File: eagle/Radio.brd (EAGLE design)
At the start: 100 x 80 mm, 134 parts, among them J500 2060-402, J501 2060-402, J920 2060-402, J921 2060-402, Q210 32.768kHz, Q610 32.768kHz, Q900 BSS123, U100 LP38693, U200 MSP430G2553, U300 IRF7103, U500 TPA2016D2, U900 EA_DOGMXXX-A, U910 PCA8574, U920 PCA9632TK, U930 IRF7309, U940 OPT3001, X100 2510-5, X110 2510-5

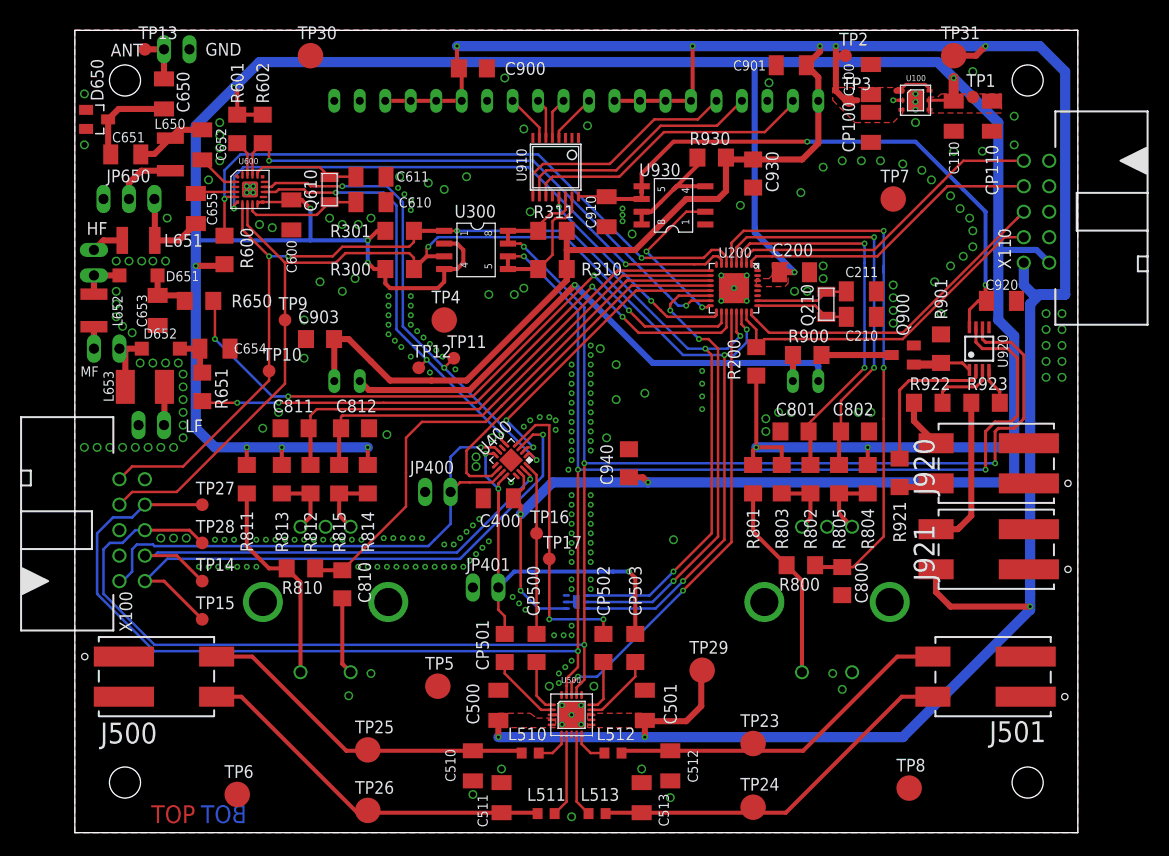
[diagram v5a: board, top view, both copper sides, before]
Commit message: CHG: updated libary pathes for all non standart components to Radio Projekt.lbr
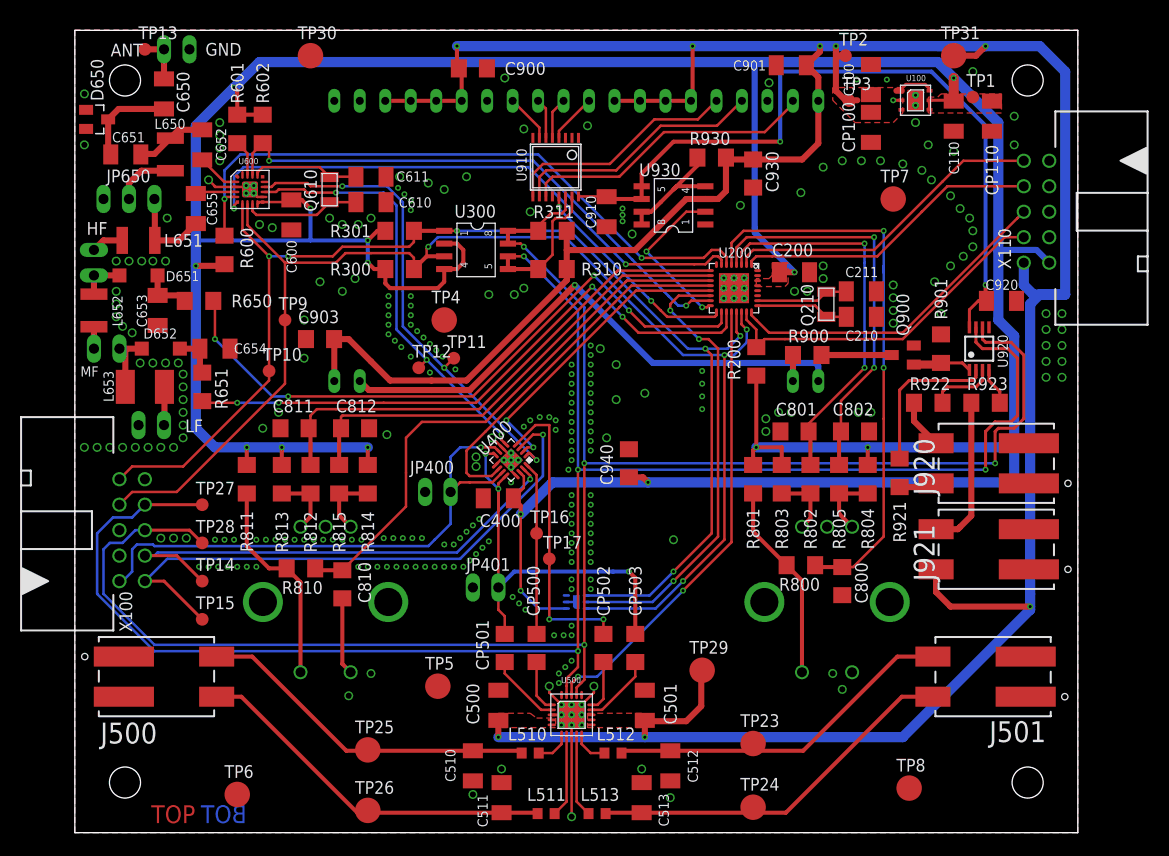
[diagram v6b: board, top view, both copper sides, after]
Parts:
- J500, J501, J920, J921: device Wago-2060-402:WAGO_2060-402 -> Radio Projekt:WAGO_2060-402
- R602: value 10k -> DNB
- U400: device TI_Radio:QFN16 -> Radio Projekt:QFN16
- U600: device SI473X-D60:SI473X-D60 -> Radio Projekt:SI473X-D60
- U920: device NXP_By_element14_Batch_1:TSSOP8 -> Radio Projekt:TSSOP8
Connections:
- net GND: now also U100.EXP1, U100.EXP2, U200.TP1, U200.TP2, U200.TP3, U200.TP4, U200.TP5, U200.TP6, U200.TP7, U200.TP8, U200.TP9, U400.TH, U400.TH1, U400.TH2, U400.TH3, U400.TH4, U400.TH5, U500.EXP1, U500.EXP2, U500.EXP3, U500.EXP4, U500.EXP5, U500.EXP6, U500.EXP7, U500.EXP8, U500.EXP9, U600.GND-PAD1, U600.GND-PAD2, U600.GND-PAD3, U600.GND-PAD4
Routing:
- net GND: track 11.5 -> 39.8 mm, vias 293 -> 278
- net +5_PCA: track 61.2 -> 75.0 mm

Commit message: CHG: added some testpads for debugging methode
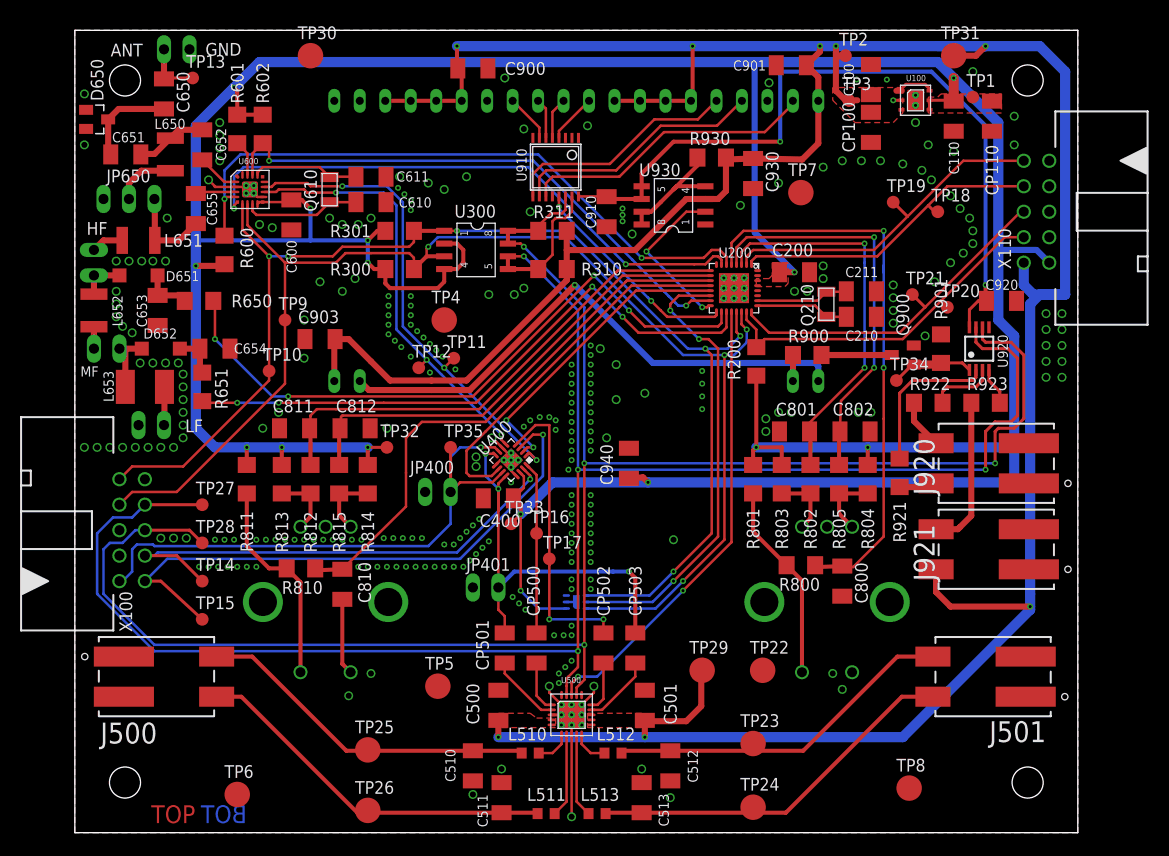
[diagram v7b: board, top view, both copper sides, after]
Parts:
- added TP18, TP19, TP20, TP21, TP32, TP33, TP34, TP35: PTR1B1,27, testpad:B1,27
- added TP22: PTR1B2,54, testpad:B2,54
- C100, C110, C200, C400, C600, C652, C653, C654, C655, C901, C910, C920, L650: value 0.1µ -> 100n
- C500, C501, CP100, CP110: value 10µ -> 10u
- C800, C801, C802, C810, C811, C812: device rcl:C1206 -> rcl:C1206K
- C900, C903, C930, CP500, CP501, CP502, CP503: value 1µ -> 1u; device rcl:C1206 -> rcl:C1206K
- C940: value 0,1µ -> 100n; device rcl:C1206 -> rcl:C1206K
- D651, D652: value (none) -> 1N4148W
- L651: value 4.7µ -> 4u7
- L652: value 220µ -> 220u
- R900: value 4.7 -> 4R7
- moved TP7 9.23 mm to (72.4, 63.8)
- moved TP13 5.55 mm to (11.7, 75.2)
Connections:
- net +3V3: now also TP32.TP, TP33.TP
- net AUX_GND: now also TP35.TP
- net GND: now also TP22.TP
- net LCD_BACKLIGHT: now also TP34.TP
- net MSP_RESET: now also TP20.TP
- net MSP_RXD: now also TP18.TP
- net MSP_TEST: now also TP21.TP
- net MSP_TXD: now also TP19.TP
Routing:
- net AUX_GND: track 54.8 -> 59.3 mm
- net +3V3: track 377.5 -> 380.8 mm
- net LCD_BACKLIGHT: track 6.00 -> 8.39 mm
- net MSP_TXD: track 32.4 -> 34.4 mm
- net MSP_TEST: track 33.2 -> 35.0 mm
- net MSP_RXD: track 30.6 -> 31.8 mm
- net ANT_FM: track 4.85 -> 5.84 mm
- net MSP_RESET: track 35.1 -> 36.0 mm
